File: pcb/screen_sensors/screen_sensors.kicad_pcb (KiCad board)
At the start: 2 copper layers, 30 x 30 mm, 18 parts, among them J1 WAVESHARE_I2C, J2 BOILER_PROBE, J3 XDB401_ANALOG, U1 ADS1115IDGSR, U2 SHT40-AD1B

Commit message: Lower the screen sensors pressure filter to 16 Hz with a 10 µF C3
The 1 kΩ / 100 nF filter only removed fast edges, letting 50/100 Hz mains
pickup alias into the ADS1115 samples once the sensor cable ran near the
230 V wiring. The design notes now record the measured sensor behaviour and
leave the 3.3 V or 5 V supply choice open.

Co-Authored-By: Claude Opus 5.5 <noreply@anthropic.com>
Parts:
- C3: value 100nF -> 10uF
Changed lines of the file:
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@@
 			)
 		)
-		(property "Value" "100nF"
+		(property "Value" "10uF"
 			(at 0 1.43 270)
 			(layer "F.Fab")
@@
 			)
 		)
-		(property "MPN" "CC0603KRX7R9BB104"
+		(property "MPN" "CL10A106KP8NNNC"
 			(at 0 0 270)
 			(layer "F.SilkS")
@@
 			)
 		)
-		(property "LCSC" "C14663"
+		(property "LCSC" "C19702"
 			(at 0 0 270)
 			(layer "F.SilkS")
@@
 			)
 		)
-		(property "Note" "Input filter at ADC; 1k/100nF fc~1.59kHz"
+		(property "Note" "Input filter at ADC; 1k/10uF fc~16Hz; X5R 10V"
 			(at 0 0 270)
 			(layer "F.SilkS")

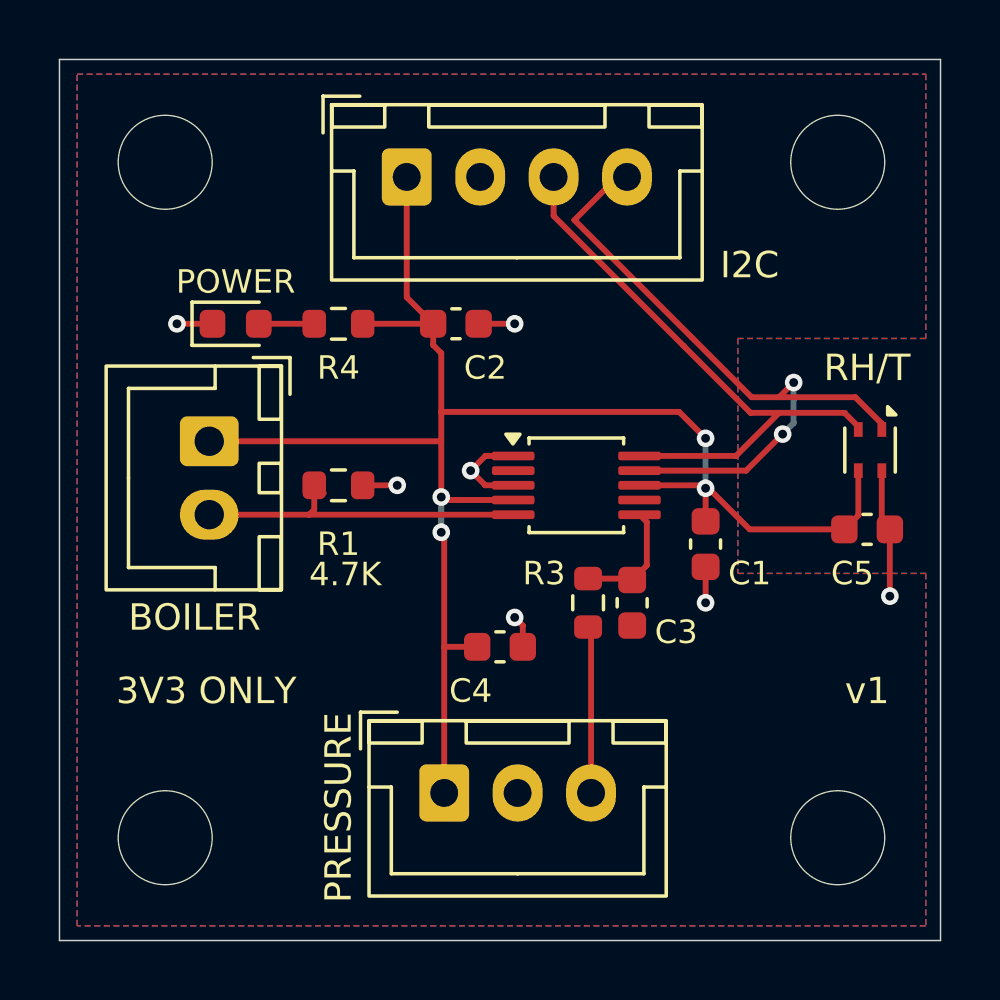
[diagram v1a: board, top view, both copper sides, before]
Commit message: Move C4 and rework the routing on the screen_sensors board
Co-Authored-By: Claude Opus 5.5 <noreply@anthropic.com>
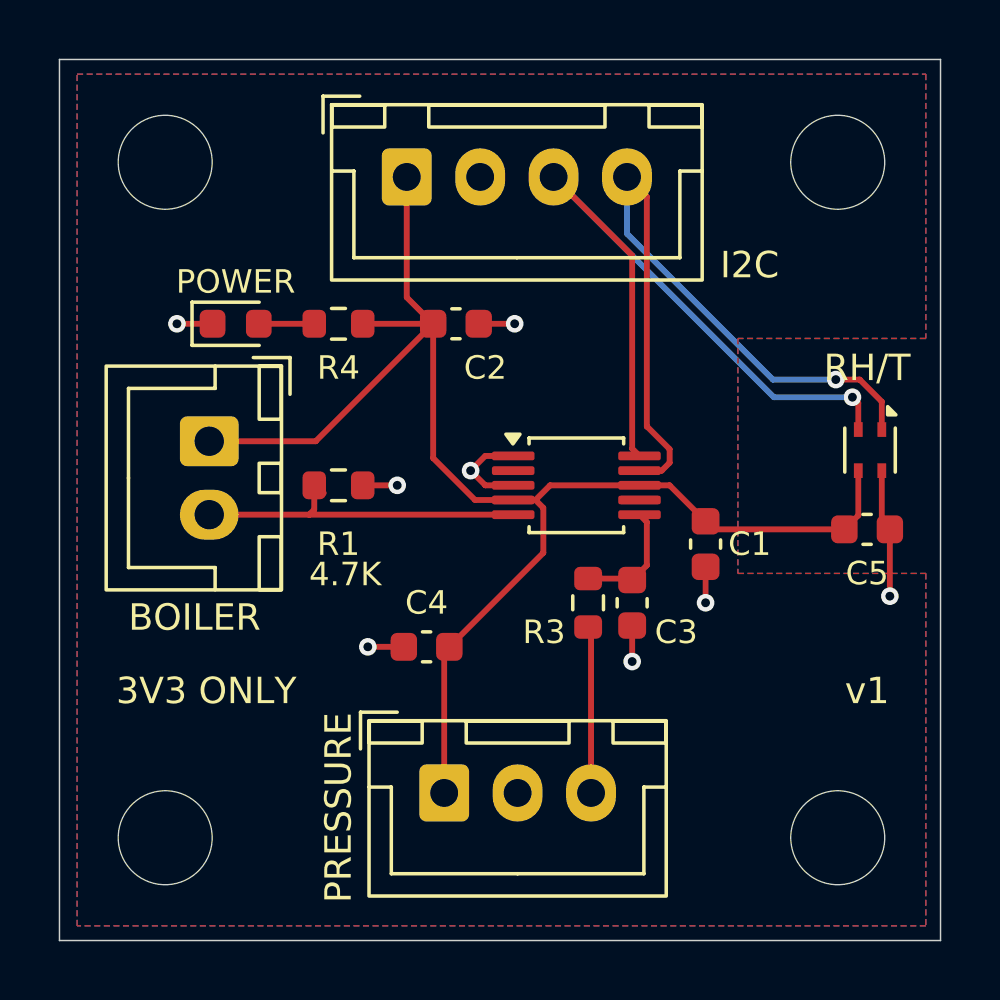
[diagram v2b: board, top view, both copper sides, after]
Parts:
- moved C4 2.50 mm to (112.5, 122.0), turned to 180 degrees
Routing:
- net /3V3: track 58.3 -> 52.4 mm, vias 4 -> 0
- net /SCL: track 20.1 -> 25.2 mm, vias 0 -> 1
- net /SDA: track 24.1 -> 25.9 mm, vias 2 -> 1
- net /GND: track 14.9 -> 16.2 mm, vias 7 -> 8
